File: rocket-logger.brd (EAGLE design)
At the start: 58.5 x 62 mm, 63 parts, among them IC1 CC430F513X, U1 MAX1555, X1 0896BM15A0001, X2 USB-MICROB, X3 SMA-142-0701-801/806

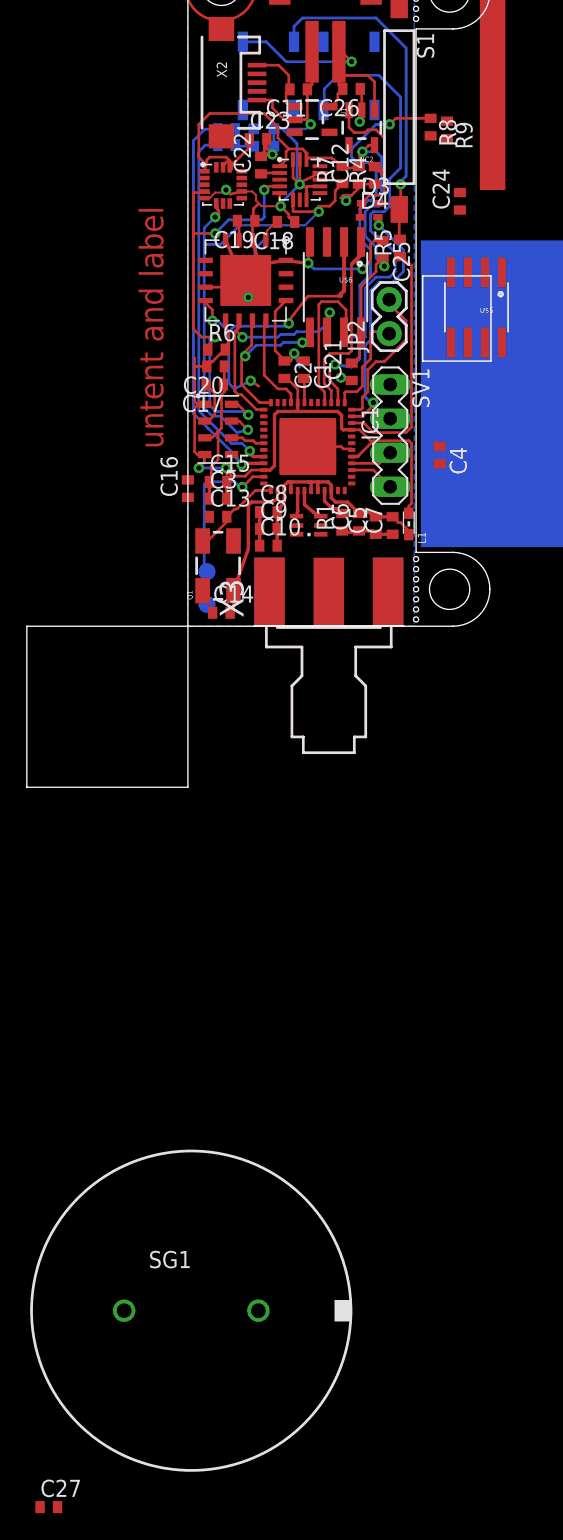
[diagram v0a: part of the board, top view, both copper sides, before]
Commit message: some routing - changed to smaller flash
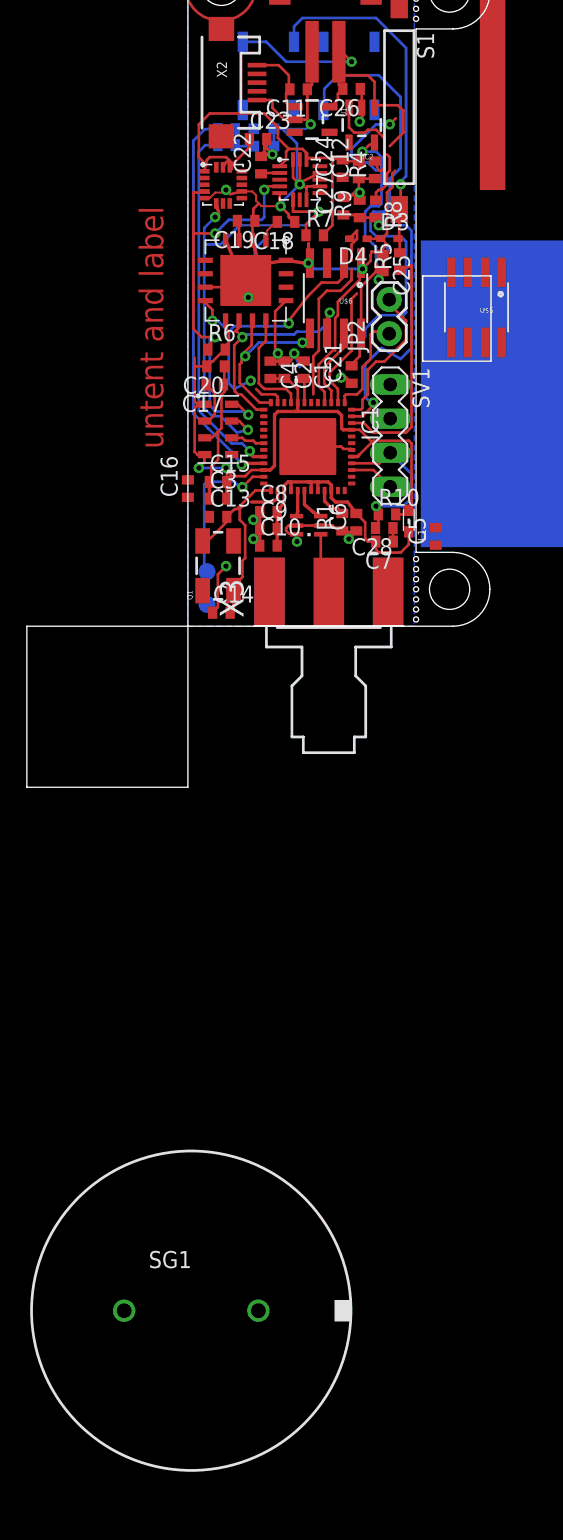
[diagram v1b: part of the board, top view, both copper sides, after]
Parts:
- added C28: (no value), resistor:C0402
- added R10: (no value), rcl:R0402
- U$6: value SPI_FLASH-X25XXSMD1 -> SPI_FLASH-X25XXSMD; device SparkFun:SO08-EIAJ -> SparkFun:SO08
- moved C27 99.4 mm to (11.6, 31.3), turned to 90 degrees
- moved C4 14.1 mm to (6.15, 19.1)
- moved C24 9.07 mm to (11.5, 34.1)
- moved R9 8.78 mm to (12.8, 31.1), turned to 90 degrees
- moved R8 7.33 mm to (14.0, 31.1)
- moved R7 4.96 mm to (9.45, 29.1), turned to 0 degrees
- moved C5 4.54 mm to (18.5, 6.69)
- moved D3 3.00 mm to (15.0, 28.9)
- moved D4 1.74 mm to (12.8, 28.9), turned to 180 degrees
- moved C7 1.33 mm to (14.6, 6.31), turned to 180 degrees
- moved C25 1.02 mm to (14.5, 27.1)
- moved R5 1.02 mm to (15.8, 27.2)
- moved U$6 0.81 mm to (11.0, 24.4)
- moved C12 0.41 mm to (12.7, 34.0)
- moved R4 0.41 mm to (13.9, 34.0)
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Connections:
- net +3V3: now also R10.2
- net GND: now also C28.1
- net N$26: now also C28.2, R10.1
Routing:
- net GND: track 113.1 -> 129.9 mm, vias 12 -> 18
- net +3V3: track 100.6 -> 111.4 mm
- net N$26: track 3.19 -> 12.1 mm, vias 0 -> 1
- net N$2: track 43.2 -> 36.0 mm
- net KEEPON: track 19.1 -> 25.0 mm
- net HOLD: track 11.7 -> 16.9 mm
- net N$8: track 0.00 -> 4.59 mm
- net N$28: track 37.3 -> 41.4 mm, vias 1 -> 0
- net MISO: track 23.9 -> 20.6 mm
- net AVCC_RF2: track 18.7 -> 21.7 mm
- net VBAT: track 0.00 -> 2.75 mm
- net SCL: track 34.2 -> 36.4 mm
- net N$25: track 12.5 -> 14.7 mm
- net SDA: track 38.0 -> 36.7 mm
- net CS: track 7.33 -> 8.43 mm

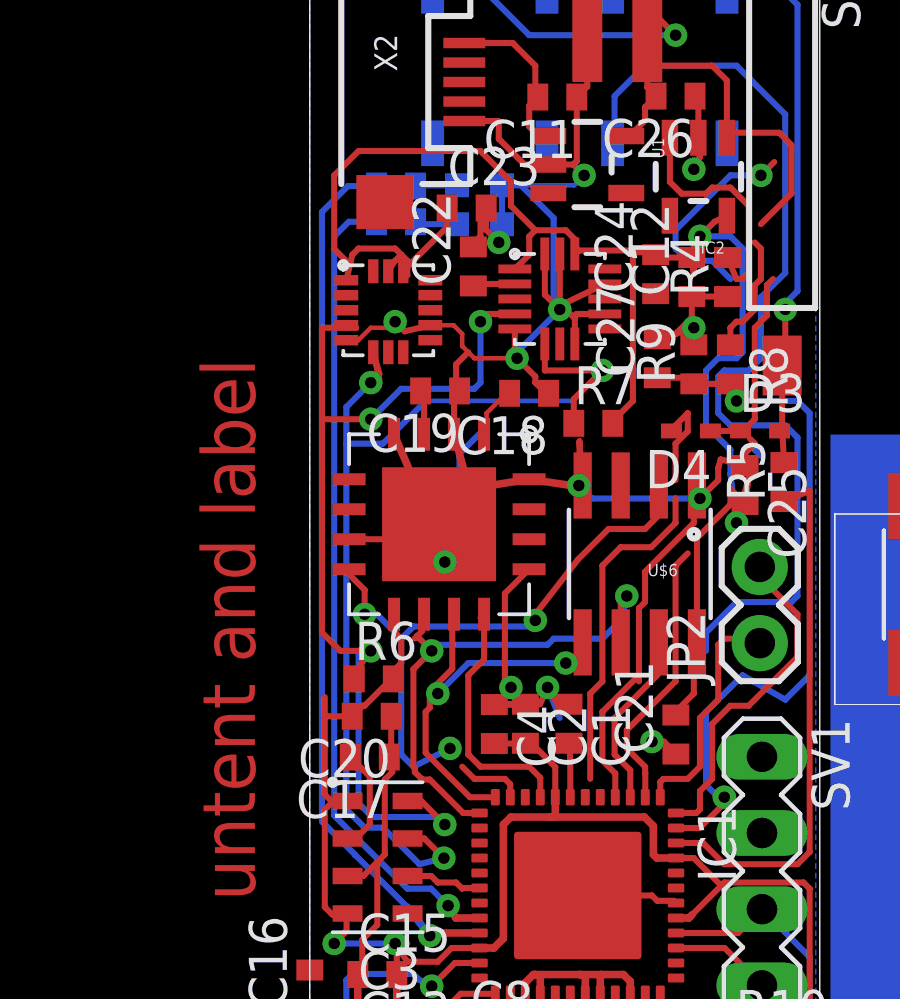
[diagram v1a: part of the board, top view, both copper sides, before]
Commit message: adding more leds
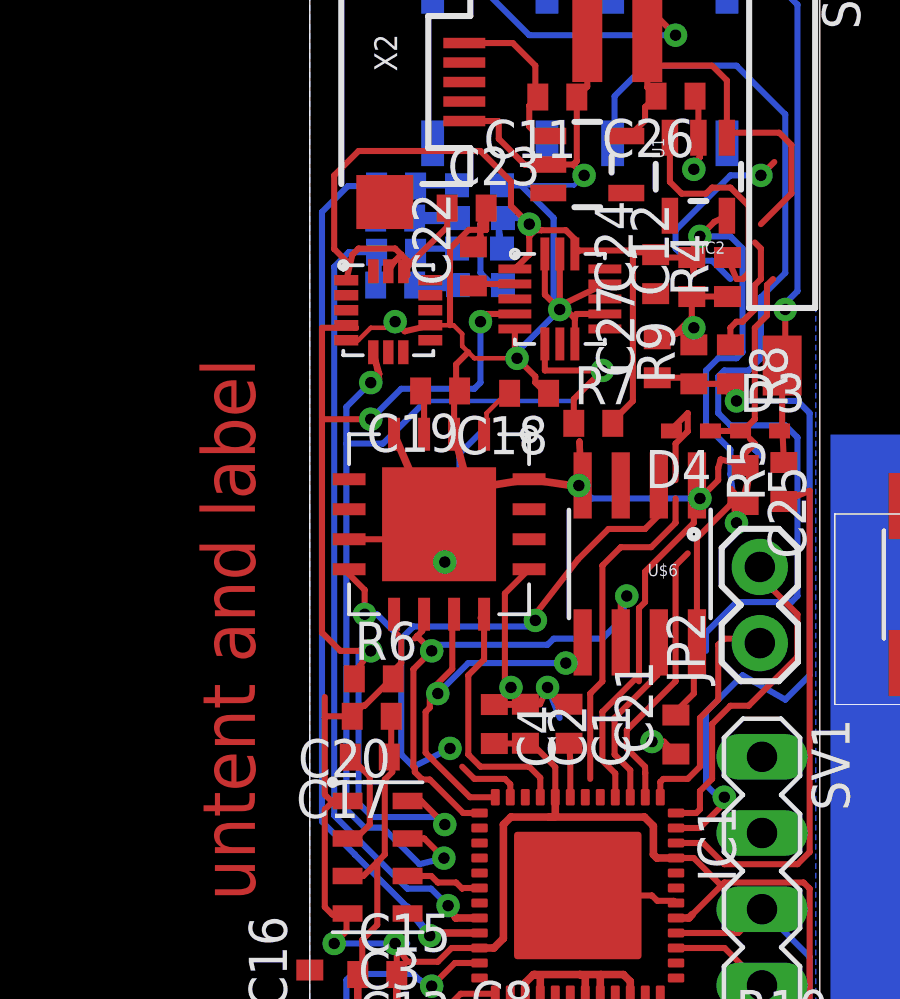
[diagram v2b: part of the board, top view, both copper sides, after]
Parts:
- added LED3, LED4: (no value), SparkFun:LED-0603
- added R11, R12: (no value), rcl:R0402
- moved R3 1.02 mm to (2.88, 34.8)
- moved LED2 0.81 mm to (5.66, 34.9)
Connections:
- new net N$18: LED3.C, R12.2
- new net N$21: LED4.C, R11.2
- net +3V3: now also LED3.A, LED4.A
- net N$16: now also R12.1
- net N$17: now also R11.1
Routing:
- net +3V3: track 111.4 -> 116.6 mm, vias 4 -> 5
- net GND: track 129.9 -> 132.5 mm, vias 18 -> 17
- net N$21: track 0.00 -> 1.44 mm
- net N$18: track 0.00 -> 1.44 mm
- net N$16: track 29.4 -> 30.5 mm

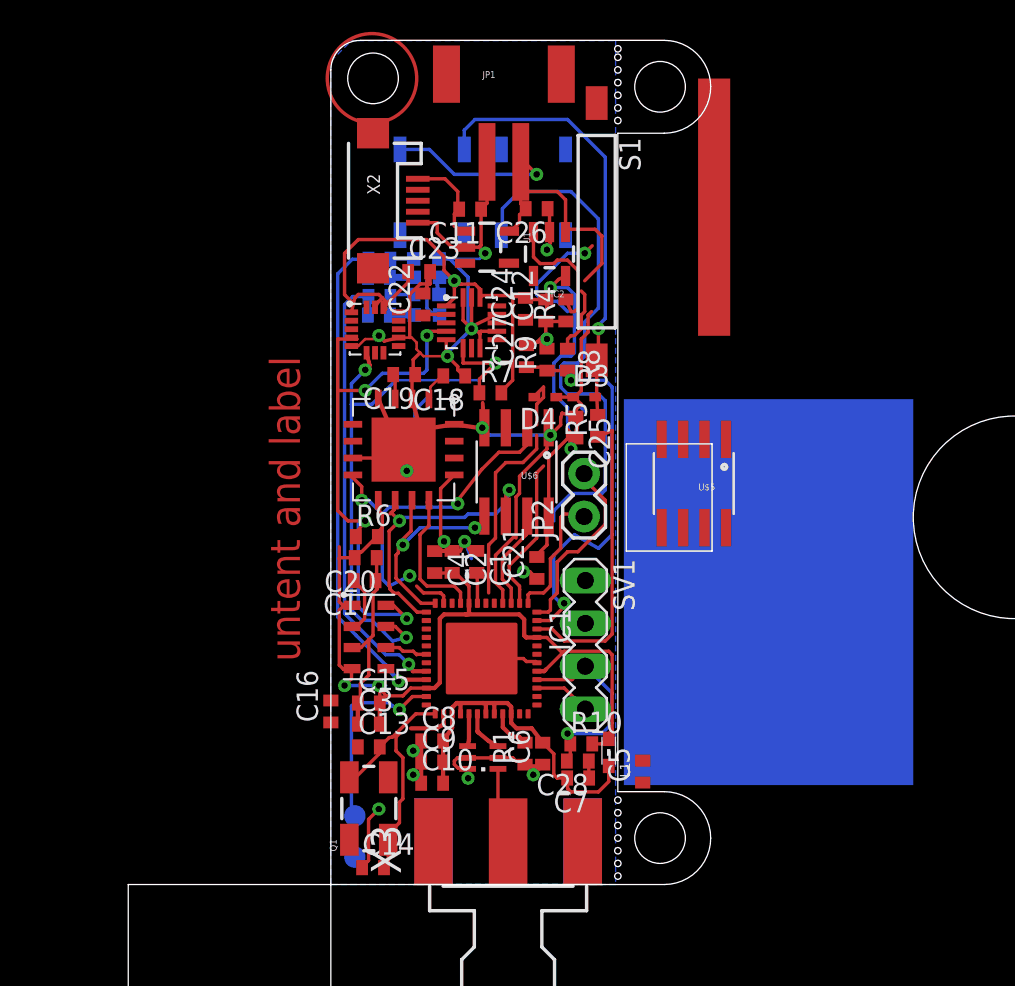
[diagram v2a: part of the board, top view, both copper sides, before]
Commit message: removed accel from simple verison, done some routing on main one
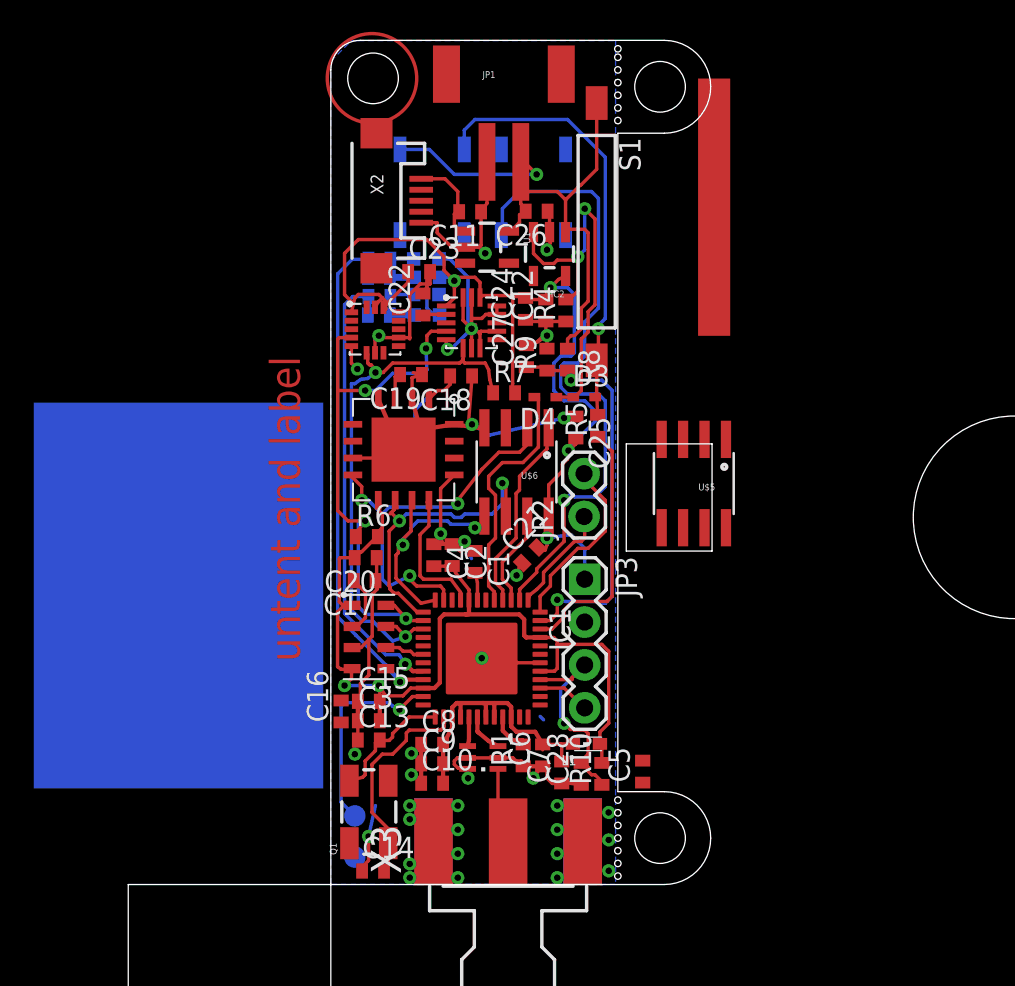
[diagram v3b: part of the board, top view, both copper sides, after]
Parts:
- removed SV1: (no value), con-lstb:MA04-1
- added JP3: (no value), SparkFun:1X04
- moved R10 2.16 mm to (16.1, 6.55), turned to 90 degrees
- moved L1 1.29 mm to (15.2, 8.33), turned to 0 degrees
- moved C7 1.03 mm to (13.7, 6.64), turned to 90 degrees
- moved C21 0.86 mm to (11.8, 19.5), turned to 45 degrees
- moved R7 0.81 mm to (10.3, 29.1)
- moved C28 0.79 mm to (14.8, 6.55), turned to 90 degrees
- moved C16 0.61 mm to (0.61, 10.2)
- moved C4 0.41 mm to (6.10, 19.5)
- moved C18 0.41 mm to (7.72, 30.1)
- moved C13 0.41 mm to (2.25, 8.56)
- moved C19 0.41 mm to (4.75, 30.2)
- moved C2 0.41 mm to (7.19, 19.5)
- moved C3 0.20 mm to (2.25, 9.70)
- moved C8 0.20 mm to (6.00, 8.30)
- moved C14 0.20 mm to (2.50, 0.80)
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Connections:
- net +3V3: now also JP3.1
- net CS_F: now also IC1.4; no longer IC1.3
- net GND: now also JP3.2
- net HOLD: now also IC1.3; no longer IC1.4
- net KEEPON: now also IC1.5; no longer IC1.47
- net MISO: now also IC1.11; no longer IC1.14
- net N$23: now also JP3.4; no longer SV1.4
- net N$26: now also JP3.3; no longer SV1.3
- net SCL: now also IC1.14; no longer IC1.11
- net SDA: now also IC1.15; no longer IC1.10
- net VBAT: now also IC1.47
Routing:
- net VBAT: track 2.75 -> 24.1 mm, vias 0 -> 2
- net KEEPON: track 25.0 -> 14.7 mm, vias 2 -> 0
- net HOLD: track 16.9 -> 6.81 mm
- net N$25: track 14.7 -> 23.3 mm, vias 0 -> 2
- net SDA: track 36.7 -> 32.6 mm, vias 3 -> 2
- net AVCC_RF2: track 21.7 -> 17.9 mm
- net MISO: track 20.6 -> 23.7 mm
- net +3V3: track 116.6 -> 119.6 mm, vias 5 -> 6
- net N$28: track 41.4 -> 38.5 mm, vias 0 -> 1
- net SWITCHON: track 17.9 -> 15.1 mm
- net SCL: track 36.4 -> 34.5 mm
- net GND: track 132.5 -> 134.1 mm, vias 17 -> 34
- net N$7: track 11.3 -> 12.8 mm
- net N$11: track 7.93 -> 6.62 mm
- net CS_F: track 13.9 -> 12.8 mm
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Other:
- board text added: "CLR MEM"
- board text added: "GRN"
- board text added: "ON/OFF"
- board text added: "RED"
- board text added: "YEL"
- board text removed: "ACT"
- board text removed: "ON"

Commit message: added charging led
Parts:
- added LED5: (no value), SparkFun:LED-0603
- added R13: (no value), rcl:R0402
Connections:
- new net N$10: R13.1, U1.3
- new net N$18: LED5.C, R13.2
- net N$1: now also LED5.A
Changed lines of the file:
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@@
 <element name="R12" library="rcl" package="R0402" value="" x="2.8448" y="35.9664" rot="MR180"/>
 <element name="JP3" library="SparkFun" package="1X04" value="" x="15.0368" y="18.0848" rot="R270"/>
+<element name="LED5" library="SparkFun" package="LED-0603" value="" x="-19.304" y="-61.3664"/>
+<element name="R13" library="rcl" package="R0402" value="" x="-18.8976" y="-65.4304"/>
 </elements>
 <signals>
@@
 <wire x1="7.3152" y1="39.0144" x2="7.3152" y2="39.7152" width="0.2032" layer="1"/>
 <wire x1="7.3152" y1="39.7152" x2="7.6" y2="39.8476" width="0.2032" layer="1"/>
+<contactref element="LED5" pad="A"/>
+<wire x1="7.6296" y1="38.7" x2="-19.304" y2="-62.1164" width="0" layer="19" extent="1-1"/>
 </signal>
 <signal name="N$2">
@@
 <contactref element="U$6" pad="5"/>
 <wire x1="9.095" y1="21.821" x2="9.095" y2="21.155" width="0.3048" layer="1"/>
-<wire x1="6.1832" y1="16.8475" x2="5.34" y2="16.66" width="0.2032" layer="1"/>
-<wire x1="5.34" y1="16.66" x2="3.8608" y2="18.1392" width="0.2032" layer="1"/>
 <wire x1="4" y1="20.1168" x2="4" y2="20.1872" width="0.2032" layer="1"/>
 <wire x1="4" y1="20.1872" x2="4.75" y2="20.9372" width="0.2032" layer="1"/>
@@
 <wire x1="4.75" y1="20.9372" x2="4.2672" y2="20.4544" width="0.2032" layer="16"/>
 <wire x1="4.2672" y1="20.1168" x2="4.2672" y2="20.4544" width="0.2032" layer="16"/>
+<wire x1="6.1832" y1="16.8475" x2="5.1525" y2="16.8475" width="0.2032" layer="1"/>
+<wire x1="5.1525" y1="16.8475" x2="3.8608" y2="18.1392" width="0.2032" layer="1"/>
 </signal>
 <signal name="CLK">
@@
 <wire x1="5.1006" y1="13.635" x2="4.9276" y2="13.6144" width="0.2032" layer="1"/>
 </signal>
-<signal name="N$18">
-<contactref element="LED3" pad="C"/>
-<contactref element="R12" pad="2"/>
-<wire x1="3.4948" y1="35.9664" x2="4.9396" y2="35.9664" width="0.4064" layer="16"/>
-</signal>
 <signal name="N$20">
 <contactref element="R3" pad="2"/>
@@
 <wire x1="3.5532" y1="37.0576" x2="3.5272" y2="37.0316" width="0.2032" layer="16"/>
 </signal>
+<signal name="N$22">
+<contactref element="LED3" pad="C"/>
+<contactref element="R12" pad="2"/>
+<wire x1="3.4948" y1="35.9664" x2="4.9396" y2="35.9664" width="0.4064" layer="16"/>
+</signal>
+<signal name="N$10">
+<contactref element="U1" pad="3"/>
+<contactref element="R13" pad="1"/>
+<wire x1="7.9499" y1="36.8" x2="-19.5476" y2="-65.4304" width="0" layer="19" extent="1-1"/>
+</signal>
+<signal name="N$18">
+<contactref element="R13" pad="2"/>
+<contactref element="LED5" pad="C"/>
+<wire x1="-19.304" y1="-60.6164" x2="-18.2476" y2="-65.4304" width="0" layer="19" extent="1-1"/>
+</signal>
 </signals>
